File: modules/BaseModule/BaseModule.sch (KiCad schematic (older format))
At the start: 58 parts, among them J1 Conn_01x04, J10 Conn_01x02_Male, J11 DB9_Female_MountingHoles, J12 Conn_01x02_Male, J13 Conn_01x02_Male, J2 Conn_01x02_Male, J3 Conn_01x04, J4 Conn_02x03_Odd_Even, J5 Conn_01x15_Male, J6 proto_grid_15x21, J7 Conn_02x02_Top_Bottom, J8 Conn_02x02_Top_Bottom, J9 Conn_01x02_Male, SW1 SW_Push, U1 STM32F103C8, U2 LM1117-5.0, U3 LM1117-3.3, U4 MAX485E, U5 MAX485E, Y1 8 MHz, Y2 32.768 KHz

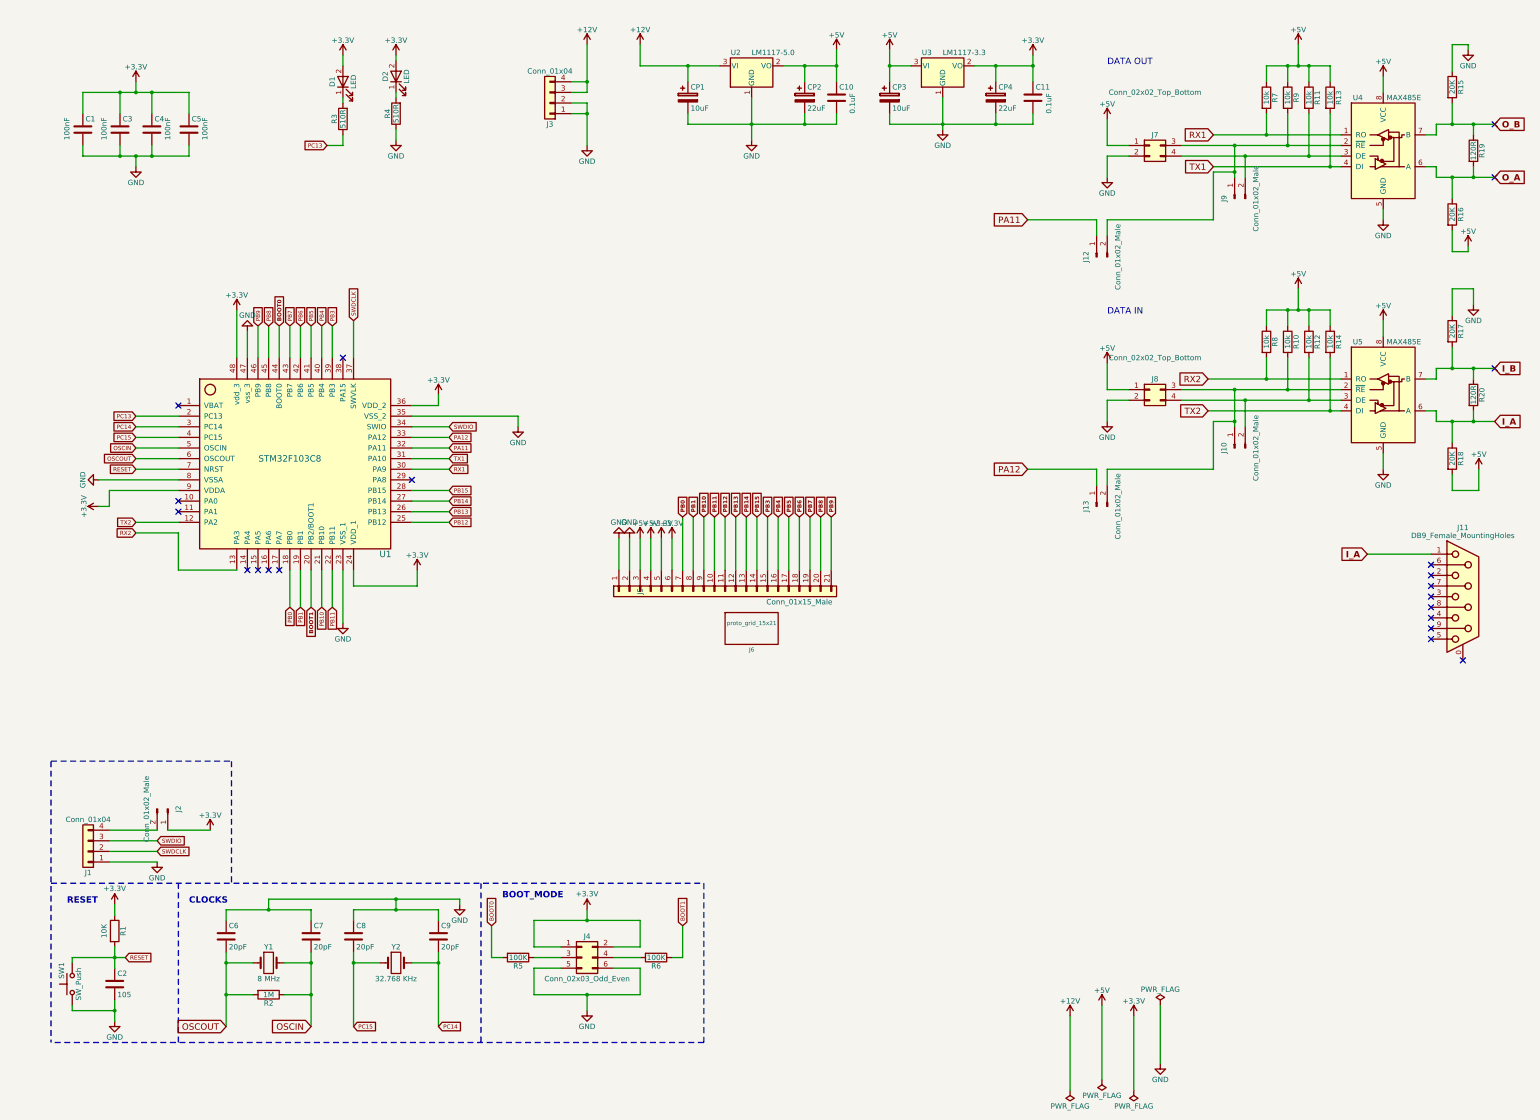
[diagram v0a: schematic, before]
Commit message: BaseModule updates and documentation updates
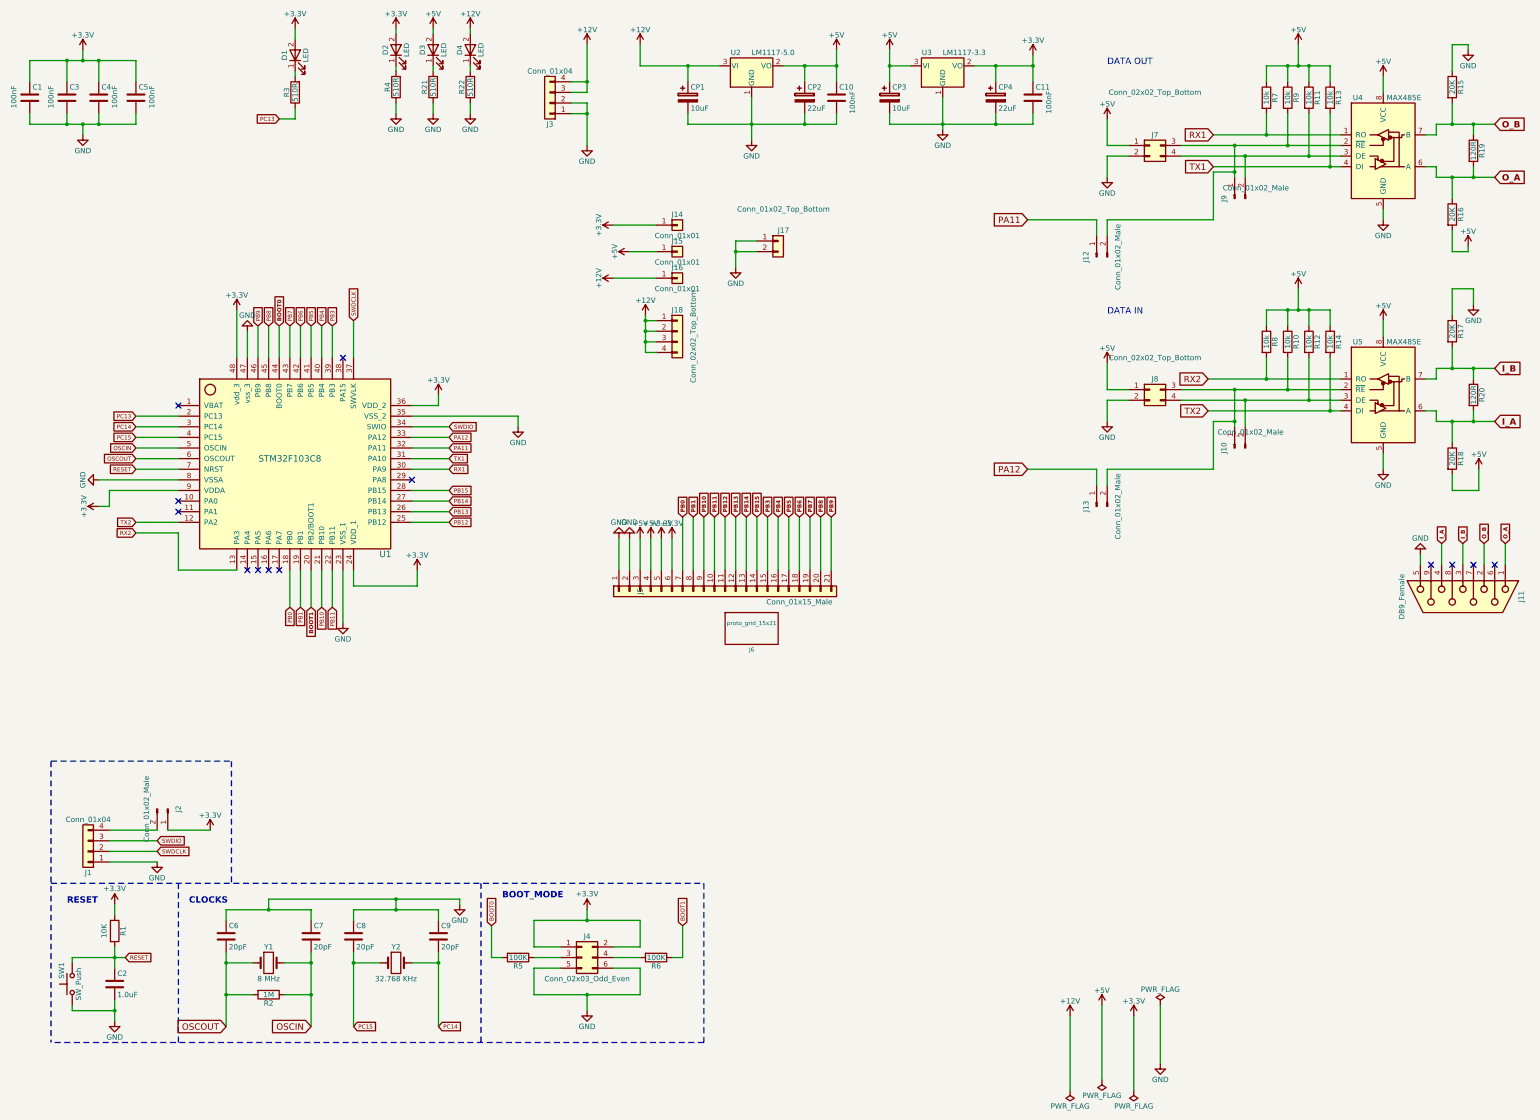
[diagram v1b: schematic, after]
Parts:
- removed J11: DB9_Female_MountingHoles, SparkFun-Connectors:DB9, symbol DB9_Female_MountingHoles
- added D3, D4: LED, LEDs:LED_0805_HandSoldering, symbol LED
- added J11: DB9_Female, symbol DB9_Female
- added J14, J15, J16: Conn_01x01, Pin_Headers:Pin_Header_Straight_1x01_Pitch2.54mm, symbol Conn_01x01
- added J17: Conn_01x02_Top_Bottom, Pin_Headers:Pin_Header_Straight_1x02_Pitch2.54mm, symbol Conn_01x02
- added J18: Conn_02x02_Top_Bottom, Socket_Strips:Socket_Strip_Straight_1x04_Pitch2.54mm, symbol Conn_01x04
- added R21, R22: 510R, Resistors_SMD:R_0603_HandSoldering, symbol R
- C10, C11: value 0.1uF -> 100nF
- C2: value 105 -> 1.0uF
- J3: footprint Connectors_Molex:Molex_MegaFit_2x02x5.70mm_Angled -> Connectors_Molex:Molex_MiniFit-JR-5569-04A2_2x02x4.20mm_Angled
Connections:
- net +12V: now also D4.2 (A), J16.1 (Pin_1), J18.1 (Pin_1), J18.2 (Pin_2), J18.3 (Pin_3), J18.4 (Pin_4)
- net +3V3: now also J14.1 (Pin_1)
- net +5V: now also D3.2 (A), J15.1 (Pin_1)
- net GND: now also J11.5, J17.1 (Pin_1), J17.2 (Pin_2), R21.1, R22.1
- net I_A: now also J11.4
- net I_B: now also J11.3
- net O_A: now also J11.1
- net O_B: now also J11.2
- new net: D3.1 (K), R21.2
- new net: D4.1 (K), R22.2
- no-connect marks 21 -> 13
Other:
- moved on the sheet: C1, C3, C4, C5, D1, D2, R3, R4
